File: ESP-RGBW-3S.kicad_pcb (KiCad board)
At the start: 2 copper layers, 66.7 x 48.3 mm, 52 parts, among them J1 12V In, J2 PROG, J3 LED Str., J4 Temp. S., J5 Light. S., J6 PIR, J91 12V In, Q1 IRLML0040TRPBF, Q2 IRLML0040TRPBF, Q3 IRLML0040TRPBF, Q4 IRLML0040TRPBF, SW1 Flash, U2 ESP-12E, U4 DCDC_LM2596, U94 MP1584

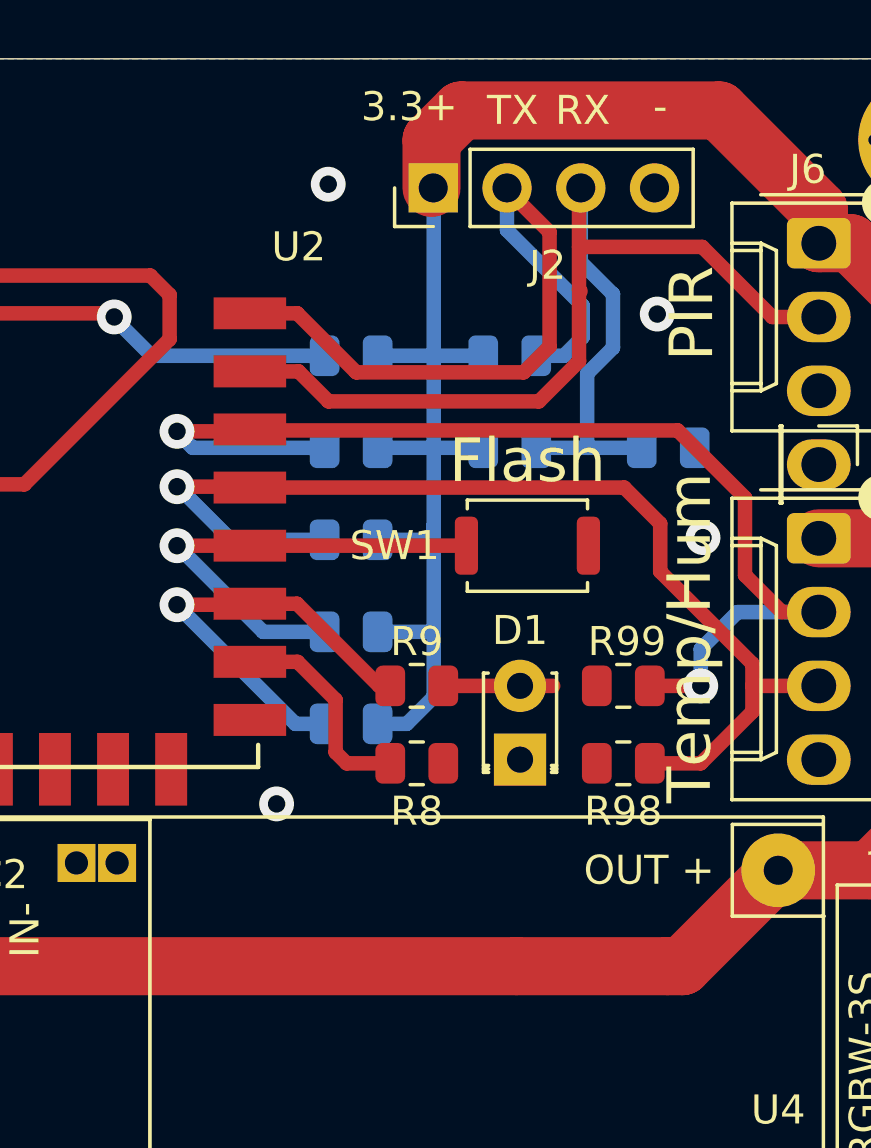
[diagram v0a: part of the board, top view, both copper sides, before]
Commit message: status LED controlled by low-velef on mcu pin
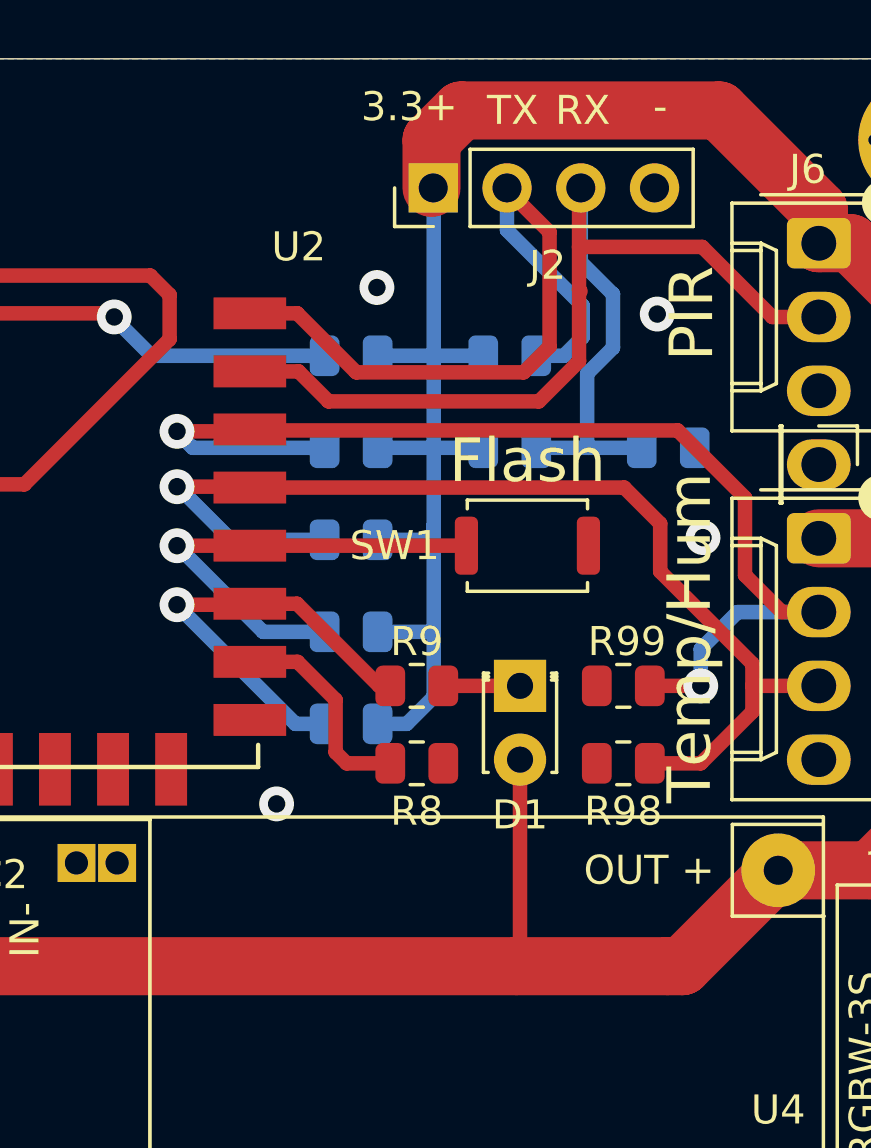
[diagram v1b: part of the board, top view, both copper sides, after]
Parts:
- R9: value 10K -> 4K7
- moved D1 2.54 mm to (69.1, 47.0), turned to 270 degrees
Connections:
- D1 pad 1: GND -> Net-(D1-Pad1)
- D1 pad 2: Net-(D1-Pad2) -> +3V3
- R9 pad 2: Net-(D1-Pad2) -> Net-(D1-Pad1)
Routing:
- net +3V3: track 206.8 -> 213.9 mm
- net Net-(D1-Pad2): track 3.67 -> 0.00 mm
- net Net-(D1-Pad1): track 0.00 -> 2.64 mm

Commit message: some hints on silk layer
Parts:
- moved IMG1 15.5 mm to (68.6, 62.2)
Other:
- board text added: "-----GPIO HINTS----- 16: H at BOOT 00: no b. if L 02: H on BOOT, no b. if L 15: no boot if H 03: H at BOOT 01: H at BOOT, no b. if L 10: H at BOOT 09: H at BOOT"

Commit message: silk layer
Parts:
- added ?: , , F.Cu at (48.8, 68.1)
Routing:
- net +12V: track 51.4 -> 56.3 mm

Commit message: Update ESP-RGBW-3S.kicad_pcb
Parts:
- moved IMG1 1.66 mm to (66.9, 62.1)
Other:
- board text added: "----GPIO HINTS----- 16: H at boot 00: no b. if L 02: H on boot, no b. if L 15: no boot if H 03: H at boot 01: H at boot, no b. if L 10: H at boot 09: H at boot"
- board text removed: "-----GPIO HINTS----- 16: H at BOOT 00: no b. if L 02: H on BOOT, no b. if L 15: no boot if H 03: H at BOOT 01: H at BOOT, no b. if L 10: H at BOOT 09: H at BOOT"
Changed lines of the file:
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@@
   (layers
     (0 F.Cu signal)
-    (31 B.Cu signal hide)
-    (32 B.Adhes user hide)
-    (33 F.Adhes user hide)
-    (34 B.Paste user hide)
+    (31 B.Cu signal)
+    (32 B.Adhes user)
+    (33 F.Adhes user)
+    (34 B.Paste user)
     (35 F.Paste user)
-    (36 B.SilkS user hide)
+    (36 B.SilkS user)
     (37 F.SilkS user)
-    (38 B.Mask user hide)
+    (38 B.Mask user)
     (39 F.Mask user)
-    (40 Dwgs.User user hide)
-    (41 Cmts.User user hide)
-    (42 Eco1.User user hide)
-    (43 Eco2.User user hide)
+    (40 Dwgs.User user)
+    (41 Cmts.User user)
+    (42 Eco1.User user)
+    (43 Eco2.User user)
     (44 Edge.Cuts user)
-    (45 Margin user hide)
-    (46 B.CrtYd user hide)
+    (45 Margin user)
+    (46 B.CrtYd user)
     (47 F.CrtYd user)
-    (48 B.Fab user hide)
+    (48 B.Fab user)
     (49 F.Fab user)
   )
@@
   )
   (module static:open-hardware-logo (layer B.Cu)
-    (at 68.58 62.23 180)
+    (at 66.929 62.103 180)
     (fp_text reference IMG1 (at 0 0) (layer B.SilkS) hide
       (effects (font (size 1.524 1.524) (thickness 0.3)) (justify mirror))
@@
     )
   )
-  (gr_text "-----GPIO HINTS-----\n16: H at BOOT\n00: no b. if L\n02: H on BOOT, no b. if L\n15: no boot if H\n03: H at BOOT\n01: H at BOOT, no b. if L\n10: H at BOOT\n09: H at BOOT\n" (at 56.388 62.611) (layer B.SilkS)
+  (gr_text "----GPIO HINTS-----\n16: H at boot\n00: no b. if L\n02: H on boot, no b. if L\n15: no boot if H\n03: H at boot\n01: H at boot, no b. if L\n10: H at boot\n09: H at boot\n" (at 56.388 62.611) (layer B.SilkS)
     (effects (font (size 1 1) (thickness 0.15)) (justify left mirror))
   )

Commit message: Update ESP-RGBW-3S.kicad_pcb
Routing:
- net +12V: track 56.3 -> 55.8 mm
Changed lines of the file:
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@@
     (thickness 1.6)
     (drawings 52)
-    (tracks 311)
+    (tracks 309)
     (zones 0)
     (modules 53)
@@
   (layers
     (0 F.Cu signal)
-    (31 B.Cu signal)
-    (32 B.Adhes user)
-    (33 F.Adhes user)
-    (34 B.Paste user)
+    (31 B.Cu signal hide)
+    (32 B.Adhes user hide)
+    (33 F.Adhes user hide)
+    (34 B.Paste user hide)
     (35 F.Paste user)
-    (36 B.SilkS user)
+    (36 B.SilkS user hide)
     (37 F.SilkS user)
-    (38 B.Mask user)
+    (38 B.Mask user hide)
     (39 F.Mask user)
-    (40 Dwgs.User user)
-    (41 Cmts.User user)
-    (42 Eco1.User user)
-    (43 Eco2.User user)
+    (40 Dwgs.User user hide)
+    (41 Cmts.User user hide)
+    (42 Eco1.User user hide)
+    (43 Eco2.User user hide)
     (44 Edge.Cuts user)
-    (45 Margin user)
-    (46 B.CrtYd user)
+    (45 Margin user hide)
+    (46 B.CrtYd user hide)
     (47 F.CrtYd user)
-    (48 B.Fab user)
+    (48 B.Fab user hide)
     (49 F.Fab user)
   )
   (setup
-    (last_trace_width 1)
+    (last_trace_width 3)
     (user_trace_width 0.5)
     (user_trace_width 1)
@@
     (mod_text_size 1 1)
     (mod_text_width 0.15)
-    (pad_size 3 3.5)
-    (pad_drill 1)
+    (pad_size 3.5 3.5)
+    (pad_drill 3)
     (pad_to_mask_clearance 0.051)
     (solder_mask_min_width 0.25)
@@
     (fp_arc (start 0 0) (end 0 1.68) (angle -24) (layer F.SilkS) (width 0.12))
     (pad 2 thru_hole circle (at 5 0 270) (size 2.6 2.6) (drill 1.3) (layers *.Cu *.Mask)
-      (net 1 GND))
+      (net 1 GND) (thermal_width 1.5))
     (pad 1 thru_hole rect (at 0 0 270) (size 2.6 2.6) (drill 1.3) (layers *.Cu *.Mask)
       (net 4 +12V))
@@
     (tags capacitor)
     (attr smd)
-    (fp_text reference C2 (at 3.1242 -0.0254) (layer F.SilkS)
+    (fp_text reference C2 (at 0.0254 1.7272) (layer F.SilkS)
       (effects (font (size 1 1) (thickness 0.15)))
     )
@@
     )
     (pad 3 thru_hole roundrect (at -3 4.7 90) (size 3.5 3.5) (drill oval 3 1) (layers *.Cu *.Mask) (roundrect_rratio 0.25)
-      (net 1 GND))
+      (net 1 GND) (thermal_width 1.5))
     (pad 2 thru_hole roundrect (at -6 0 90) (size 3 3.5) (drill oval 1 3) (layers *.Cu *.Mask) (roundrect_rratio 0.25)
       (net 1 GND) (thermal_width 1.5))
@@
   (via (at 33.274 50.546) (size 1.2) (drill 0.6) (layers F.Cu B.Cu) (net 1))
   (via (at 60.706 51.054) (size 1.2) (drill 0.6) (layers F.Cu B.Cu) (net 1))
-  (via (at 64.1604 33.274) (size 1.2) (drill 0.6) (layers F.Cu B.Cu) (net 1))
+  (via (at 64.1604 32.766) (size 1.2) (drill 0.6) (layers F.Cu B.Cu) (net 1))
   (via (at 75.3872 41.8846) (size 1.2) (drill 0.6) (layers F.Cu B.Cu) (net 1))
   (segment (start 34.541058 28.196942) (end 34.541058 30.381342) (width 0.5) (layer F.Cu) (net 2))
@@
   (segment (start 69.088 56.515) (end 68.961 56.642) (width 0.5) (layer F.Cu) (net 3))
   (segment (start 69.088 49.53) (end 69.088 56.515) (width 0.5) (layer F.Cu) (net 3))
-  (segment (start 24.638 32.258) (end 24.68599 32.30599) (width 3) (layer B.Cu) (net 4))
-  (segment (start 24.68599 32.30599) (end 25.146 32.30599) (width 3) (layer B.Cu) (net 4))
-  (segment (start 23.905193 32.258) (end 24.638 32.258) (width 3) (layer B.Cu) (net 4))
-  (segment (start 21.59 34.573193) (end 23.905193 32.258) (width 3) (layer B.Cu) (net 4))
-  (segment (start 21.59 56.066) (end 21.59 34.573193) (width 3) (layer B.Cu) (net 4))
-  (segment (start 21.59 56.066) (end 21.649 56.066) (width 3) (layer B.Cu) (net 4))
-  (segment (start 21.649 56.066) (end 25.019 59.436) (width 3) (layer B.Cu) (net 4))
   (segment (start 33.909 53.34) (end 37.338 53.34) (width 2) (layer B.Cu) (net 4))
   (segment (start 29.21 58.039) (end 33.909 53.34) (width 2) (layer B.Cu) (net 4))
@@
   (segment (start 39.1146 53.0874) (end 40.7446 53.0874) (width 1) (layer B.Cu) (net 4))
   (segment (start 38.862 53.34) (end 39.1146 53.0874) (width 1) (layer B.Cu) (net 4))
-  (segment (start 25.019 59.436) (end 29.21 59.436) (width 2) (layer F.Cu) (net 4))
   (segment (start 40.7446 53.0874) (end 42.1446 53.0874) (width 2) (layer B.Cu) (net 4))
   (segment (start 37.338 53.34) (end 38.735 53.34) (width 1) (layer F.Cu) (net 4))
   (segment (start 38.9876 53.0874) (end 42.1446 53.0874) (width 1) (layer F.Cu) (net 4))
   (segment (start 38.735 53.34) (end 38.9876 53.0874) (width 1) (layer F.Cu) (net 4))
+  (segment (start 25.019 59.436) (end 29.21 59.436) (width 3.5) (layer B.Cu) (net 4))
+  (segment (start 23.905193 32.258) (end 24.638 32.258) (width 3) (layer B.Cu) (net 4))
+  (segment (start 21.59 34.573193) (end 23.905193 32.258) (width 3) (layer B.Cu) (net 4))
+  (segment (start 21.59 56.066) (end 21.59 34.573193) (width 3) (layer B.Cu) (net 4))
+  (segment (start 21.649 56.066) (end 21.59 56.066) (width 3) (layer B.Cu) (net 4))
+  (segment (start 25.019 59.436) (end 21.649 56.066) (width 3) (layer B.Cu) (net 4))
   (segment (start 68.639399 31.301399) (end 68.639399 29.845) (width 0.5) (layer B.Cu) (net 5))
   (segment (start 71.247 34.9758) (end 71.247 33.909) (width 0.5) (layer B.Cu) (net 5))

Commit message: gerber files
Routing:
- net Blue: track 16.1 -> 17.0 mm

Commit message: .
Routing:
- net +3V3: track 213.9 -> 215.9 mm
